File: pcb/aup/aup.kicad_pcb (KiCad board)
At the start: 8 copper layers, 81 x 50 mm, 83 parts, among them IC1 MT41K128M16JT-125_K, J1 QSH-060-01-L-D-A, J2 QSH-060-01-L-D-A, Q2 AO3400A, Q3 AO3401A, U1 XC7A50T-FGG484, U10 TPS2116DRLR, U11 FT2232HQ, U12 93LC56BT-I/OT, U13 MX25L3233FM2, U14 ISL80103IRAJZ-TK, U15 TPS2116DRLR, U2 USBLC6-2SC6, U5 TPS563257DRLR, U6 ISL80103IRAJZ-TK, U7 TPS563257DRLR, U8 TPS563257DRLR, U9 TPS563257DRLR, Y1 12MHz/20pf

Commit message: Add upper connector
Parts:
- added J3: QTH-060-01-L-D-A, !Misc:SAMTEC_QTH-060-01-X-D-A, B.Cu at (70.2, 75.0)
- added J4: QTH-060-01-L-D-A, !Misc:SAMTEC_QTH-060-01-X-D-A, B.Cu at (109.8, 75.0)
- added J5: QSH-030-01-L-D-A, !Misc:SAMTEC_QSH-030-01-X-D-A, F.Cu at (90.0, 55.4)
- added J6: QTH-030-01-L-D-A, !Misc:SAMTEC_QTH-030-01-X-D-A, B.Cu at (90.0, 55.4)
- moved FB1 138.7 mm to (264.4, 105.3)
- moved FB2 138.7 mm to (264.4, 109.3)
- moved R25 138.7 mm to (270.6, 94.2)
- moved R26 138.7 mm to (270.6, 90.7)
- moved U13 138.7 mm to (264.4, 75.4)
- moved Y1 138.7 mm to (276.4, 102.4)
- moved C1 138.7 mm to (165.0, 50.4)
- moved C11 138.7 mm to (196.8, 88.5)
- moved C12 138.7 mm to (196.8, 86.5)
- moved C13 138.7 mm to (193.9, 56.4)
- moved C14 138.7 mm to (200.0, 88.5)
- moved C15 138.7 mm to (193.8, 49.9)
- moved C16 138.7 mm to (203.4, 49.8)
- moved C17 138.7 mm to (203.6, 56.2)
- moved C19 138.7 mm to (198.2, 94.1)
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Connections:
- J1 pad 10: unconnected-(J1-Pad10) -> +3V3
- J1 pad 100: unconnected-(J1-Pad100) -> IOL_17B
- J1 pad 101: unconnected-(J1-Pad101) -> +3V3
- J1 pad 102: unconnected-(J1-Pad102) -> +3V3
- J1 pad 103: unconnected-(J1-Pad103) -> IOL_7A
- J1 pad 104: unconnected-(J1-Pad104) -> IOL_20B
- J1 pad 105: unconnected-(J1-Pad105) -> IOL_21A
- J1 pad 106: unconnected-(J1-Pad106) -> IOL_18B
- J1 pad 107: unconnected-(J1-Pad107) -> IOL_12A
- J1 pad 108: unconnected-(J1-Pad108) -> IOL_21B
- J1 pad 109: unconnected-(J1-Pad109) -> IOL_26B
- J1 pad 11: unconnected-(J1-Pad11) -> IOT_181
- J1 pad 110: unconnected-(J1-Pad110) -> IOL_24A
- J1 pad 111: unconnected-(J1-Pad111) -> +3V3
- J1 pad 112: unconnected-(J1-Pad112) -> +3V3
- J1 pad 113: unconnected-(J1-Pad113) -> IOL_25B
- J1 pad 114: unconnected-(J1-Pad114) -> IOL_25A
- J1 pad 115: unconnected-(J1-Pad115) -> IOL_16B
- J1 pad 116: unconnected-(J1-Pad116) -> IOL_26A
- J1 pad 117: unconnected-(J1-Pad117) -> IOL_22A
- J1 pad 118: unconnected-(J1-Pad118) -> IOL_22B
- J1 pad 119: unconnected-(J1-Pad119) -> IOL_19B
- J1 pad 12: unconnected-(J1-Pad12) -> IOT_182
- J1 pad 120: unconnected-(J1-Pad120) -> IOL_24B
- J1 pad 13: unconnected-(J1-Pad13) -> IOT_185
- J1 pad 14: unconnected-(J1-Pad14) -> IOT_187
- J1 pad 15: unconnected-(J1-Pad15) -> IOT_179
- J1 pad 16: unconnected-(J1-Pad16) -> IOT_169
- J1 pad 17: unconnected-(J1-Pad17) -> IOT_193
- J1 pad 18: unconnected-(J1-Pad18) -> IOT_184
- J1 pad 19: unconnected-(J1-Pad19) -> +3V3
- J1 pad 20: unconnected-(J1-Pad20) -> +3V3
- J1 pad 21: unconnected-(J1-Pad21) -> IOT_191
- J1 pad 22: unconnected-(J1-Pad22) -> IOT_168
- J1 pad 23: unconnected-(J1-Pad23) -> IOT_192
- J1 pad 24: unconnected-(J1-Pad24) -> IOT_186
- J1 pad 25: unconnected-(J1-Pad25) -> IOT_209
- J1 pad 26: unconnected-(J1-Pad26) -> IOT_183
- J1 pad 27: unconnected-(J1-Pad27) -> IOT_200
- J1 pad 28: unconnected-(J1-Pad28) -> IOT_194
- J1 pad 29: unconnected-(J1-Pad29) -> +3V3
- J1 pad 30: unconnected-(J1-Pad30) -> +3V3
- J1 pad 31: unconnected-(J1-Pad31) -> IOT_197
- J1 pad 32: unconnected-(J1-Pad32) -> IOT_177
- J1 pad 33: unconnected-(J1-Pad33) -> IOT_219
- J1 pad 34: unconnected-(J1-Pad34) -> IOT_199
- J1 pad 35: unconnected-(J1-Pad35) -> IOT_210
- J1 pad 36: unconnected-(J1-Pad36) -> IOT_203
- J1 pad 37: unconnected-(J1-Pad37) -> IOT_221
- J1 pad 38: unconnected-(J1-Pad38) -> IOT_205
- J1 pad 39: unconnected-(J1-Pad39) -> +3V3
- J1 pad 40: unconnected-(J1-Pad40) -> +3V3
- J1 pad 41: unconnected-(J1-Pad41) -> IOT_222
- J1 pad 42: unconnected-(J1-Pad42) -> IOT_207
- J1 pad 43: unconnected-(J1-Pad43) -> IOT_206
- J1 pad 44: unconnected-(J1-Pad44) -> IOT_211
- J1 pad 45: unconnected-(J1-Pad45) -> IOT_227
- J1 pad 46: unconnected-(J1-Pad46) -> IOT_208
- J1 pad 47: unconnected-(J1-Pad47) -> IOT_198
- J1 pad 48: unconnected-(J1-Pad48) -> IOT_216
- J1 pad 49: unconnected-(J1-Pad49) -> +3V3
- J1 pad 50: unconnected-(J1-Pad50) -> +3V3
- J1 pad 51: unconnected-(J1-Pad51) -> IOT_212
- J1 pad 52: unconnected-(J1-Pad52) -> IOT_213
- J1 pad 53: unconnected-(J1-Pad53) -> IOT_224
- J1 pad 54: unconnected-(J1-Pad54) -> IOT_214
- J1 pad 55: unconnected-(J1-Pad55) -> IOT_215
- J1 pad 56: unconnected-(J1-Pad56) -> IOT_223
- J1 pad 57: unconnected-(J1-Pad57) -> IOT_226
- J1 pad 58: unconnected-(J1-Pad58) -> IOT_218
- J1 pad 59: unconnected-(J1-Pad59) -> IOT_225
- J1 pad 60: unconnected-(J1-Pad60) -> IOT_220
- J1 pad 61: unconnected-(J1-Pad61) -> IOL_2A
- J1 pad 62: unconnected-(J1-Pad62) -> IOL_1B
- J1 pad 63: unconnected-(J1-Pad63) -> IOL_1A
- J1 pad 64: unconnected-(J1-Pad64) -> IOL_2B
- J1 pad 65: unconnected-(J1-Pad65) -> IOL_5A
- J1 pad 66: unconnected-(J1-Pad66) -> IOL_3B
- J1 pad 67: unconnected-(J1-Pad67) -> IOL_6B
- J1 pad 68: unconnected-(J1-Pad68) -> IOL_3A
- J1 pad 69: unconnected-(J1-Pad69) -> IOL_10A
- J1 pad 70: unconnected-(J1-Pad70) -> IOL_4B
- J1 pad 71: unconnected-(J1-Pad71) -> +3V3
- J1 pad 72: unconnected-(J1-Pad72) -> +3V3
- J1 pad 73: unconnected-(J1-Pad73) -> IOL_19A
- J1 pad 74: unconnected-(J1-Pad74) -> IOL_5B
- J1 pad 75: unconnected-(J1-Pad75) -> IOL_8B
- J1 pad 76: unconnected-(J1-Pad76) -> IOL_10B
- J1 pad 77: unconnected-(J1-Pad77) -> IOL_13A
- J1 pad 78: unconnected-(J1-Pad78) -> IOL_9B
- J1 pad 79: unconnected-(J1-Pad79) -> IOL_4A
- J1 pad 80: unconnected-(J1-Pad80) -> IOL_13B
- J1 pad 81: unconnected-(J1-Pad81) -> +3V3
- J1 pad 82: unconnected-(J1-Pad82) -> +3V3
- J1 pad 83: unconnected-(J1-Pad83) -> IOL_8A
- J1 pad 84: unconnected-(J1-Pad84) -> IOL_11B
- J1 pad 85: unconnected-(J1-Pad85) -> IOL_20A
- J1 pad 86: unconnected-(J1-Pad86) -> IOL_14B
- J1 pad 87: unconnected-(J1-Pad87) -> IOL_6A
- J1 pad 88: unconnected-(J1-Pad88) -> IOL_12B
- J1 pad 89: unconnected-(J1-Pad89) -> IOL_18A
- J1 pad 90: unconnected-(J1-Pad90) -> IOL_7B
- J1 pad 91: unconnected-(J1-Pad91) -> +3V3
- J1 pad 92: unconnected-(J1-Pad92) -> +3V3
- J1 pad 93: unconnected-(J1-Pad93) -> IOL_23A
- J1 pad 94: unconnected-(J1-Pad94) -> IOL_15B
- J1 pad 95: unconnected-(J1-Pad95) -> IOL_9A
- J1 pad 96: unconnected-(J1-Pad96) -> IOL_15A
- J1 pad 97: unconnected-(J1-Pad97) -> IOL_17A
- J1 pad 98: unconnected-(J1-Pad98) -> IOL_16A
- J1 pad 99: unconnected-(J1-Pad99) -> IOL_11A
- J2 pad 10: unconnected-(J2-Pad10) -> +3V3
- J2 pad 100: unconnected-(J2-Pad100) -> IOB_67
- J2 pad 101: unconnected-(J2-Pad101) -> +3V3
- J2 pad 102: unconnected-(J2-Pad102) -> +3V3
- J2 pad 103: unconnected-(J2-Pad103) -> IOB_75
- J2 pad 104: unconnected-(J2-Pad104) -> IOB_52
- J2 pad 105: unconnected-(J2-Pad105) -> IOB_53
- J2 pad 106: unconnected-(J2-Pad106) -> IOB_82
- J2 pad 107: unconnected-(J2-Pad107) -> IOB_73
- J2 pad 108: unconnected-(J2-Pad108) -> IOB_56
- J2 pad 109: unconnected-(J2-Pad109) -> IOB_71
- J2 pad 11: unconnected-(J2-Pad11) -> IOR_157
- J2 pad 110: unconnected-(J2-Pad110) -> IOB_77
- J2 pad 111: unconnected-(J2-Pad111) -> +3V3
- J2 pad 112: unconnected-(J2-Pad112) -> +3V3
- J2 pad 113: unconnected-(J2-Pad113) -> IOB_69
- J2 pad 114: unconnected-(J2-Pad114) -> IOB_64
- J2 pad 115: unconnected-(J2-Pad115) -> IOB_63
- J2 pad 116: unconnected-(J2-Pad116) -> IOB_54
- J2 pad 117: unconnected-(J2-Pad117) -> IOB_61
- J2 pad 118: unconnected-(J2-Pad118) -> IOB_58
- J2 pad 119: unconnected-(J2-Pad119) -> IOB_57
- J2 pad 12: unconnected-(J2-Pad12) -> IOR_160
- J2 pad 120: unconnected-(J2-Pad120) -> IOL_23B
- J2 pad 13: unconnected-(J2-Pad13) -> IOR_151
- J2 pad 14: unconnected-(J2-Pad14) -> IOR_150
- J2 pad 15: unconnected-(J2-Pad15) -> IOR_147
- J2 pad 16: unconnected-(J2-Pad16) -> IOR_155
- J2 pad 17: unconnected-(J2-Pad17) -> IOR_149
- J2 pad 18: unconnected-(J2-Pad18) -> IOR_146
- J2 pad 19: unconnected-(J2-Pad19) -> +3V3
- J2 pad 20: unconnected-(J2-Pad20) -> +3V3
- J2 pad 21: unconnected-(J2-Pad21) -> IOR_145
- J2 pad 22: unconnected-(J2-Pad22) -> IOR_144
- J2 pad 23: unconnected-(J2-Pad23) -> IOR_143
- J2 pad 24: unconnected-(J2-Pad24) -> IOR_152
- J2 pad 25: unconnected-(J2-Pad25) -> IOR_130
- J2 pad 26: unconnected-(J2-Pad26) -> IOR_140
- J2 pad 27: unconnected-(J2-Pad27) -> IOR_138
- J2 pad 28: unconnected-(J2-Pad28) -> IOR_142
- J2 pad 29: unconnected-(J2-Pad29) -> +3V3
- J2 pad 30: unconnected-(J2-Pad30) -> +3V3
- J2 pad 31: unconnected-(J2-Pad31) -> IOR_141
- J2 pad 32: unconnected-(J2-Pad32) -> IOR_139
- J2 pad 33: unconnected-(J2-Pad33) -> IOR_131
- J2 pad 34: unconnected-(J2-Pad34) -> IOR_136
- J2 pad 35: unconnected-(J2-Pad35) -> IOR_133
- J2 pad 36: unconnected-(J2-Pad36) -> IOR_122
- J2 pad 37: unconnected-(J2-Pad37) -> IOR_129
- J2 pad 38: unconnected-(J2-Pad38) -> IOR_126
- J2 pad 39: unconnected-(J2-Pad39) -> +3V3
- J2 pad 40: unconnected-(J2-Pad40) -> +3V3
- J2 pad 41: unconnected-(J2-Pad41) -> IOR_127
- J2 pad 42: unconnected-(J2-Pad42) -> IOR_116
- J2 pad 43: unconnected-(J2-Pad43) -> IOR_119
- J2 pad 44: unconnected-(J2-Pad44) -> IOR_137
- J2 pad 45: unconnected-(J2-Pad45) -> IOR_121
- J2 pad 46: unconnected-(J2-Pad46) -> IOR_114
- J2 pad 47: unconnected-(J2-Pad47) -> IOR_109
- J2 pad 48: unconnected-(J2-Pad48) -> IOR_134
- J2 pad 49: unconnected-(J2-Pad49) -> +3V3
- J2 pad 50: unconnected-(J2-Pad50) -> +3V3
- J2 pad 51: unconnected-(J2-Pad51) -> IOR_123
- J2 pad 52: unconnected-(J2-Pad52) -> IOR_120
- J2 pad 53: unconnected-(J2-Pad53) -> IOR_117
- J2 pad 54: unconnected-(J2-Pad54) -> IOR_115
- J2 pad 55: unconnected-(J2-Pad55) -> IOR_112
- J2 pad 56: unconnected-(J2-Pad56) -> IOR_128
- J2 pad 57: unconnected-(J2-Pad57) -> IOR_113
- J2 pad 58: unconnected-(J2-Pad58) -> IOR_111
- J2 pad 59: unconnected-(J2-Pad59) -> IOR_110
- J2 pad 60: unconnected-(J2-Pad60) -> IOR_118
- J2 pad 61: unconnected-(J2-Pad61) -> IOB_102
- J2 pad 62: unconnected-(J2-Pad62) -> IOB_101
- J2 pad 63: unconnected-(J2-Pad63) -> IOB_100
- J2 pad 64: unconnected-(J2-Pad64) -> IOB_98
- J2 pad 65: unconnected-(J2-Pad65) -> IOB_91
- J2 pad 66: unconnected-(J2-Pad66) -> IOB_93
- J2 pad 67: unconnected-(J2-Pad67) -> IOB_92
- J2 pad 68: unconnected-(J2-Pad68) -> IOB_105_SDO
- J2 pad 69: unconnected-(J2-Pad69) -> IOB_103_CBSEL1
- J2 pad 70: unconnected-(J2-Pad70) -> IOB_106_SDI
- J2 pad 71: unconnected-(J2-Pad71) -> +3V3
- J2 pad 72: unconnected-(J2-Pad72) -> +3V3
- J2 pad 73: unconnected-(J2-Pad73) -> IOB_60
- J2 pad 74: unconnected-(J2-Pad74) -> IOB_87
- J2 pad 75: unconnected-(J2-Pad75) -> IOB_94
- J2 pad 76: unconnected-(J2-Pad76) -> IOB_86
- J2 pad 77: unconnected-(J2-Pad77) -> IOB_107_SCK
- J2 pad 78: unconnected-(J2-Pad78) -> IOB_99
- J2 pad 79: unconnected-(J2-Pad79) -> IOB_89
- J2 pad 80: unconnected-(J2-Pad80) -> IOB_85
- J2 pad 81: unconnected-(J2-Pad81) -> +3V3
- J2 pad 82: unconnected-(J2-Pad82) -> +3V3
- J2 pad 83: unconnected-(J2-Pad83) -> IOB_84
- J2 pad 84: unconnected-(J2-Pad84) -> IOB_74
- J2 pad 85: unconnected-(J2-Pad85) -> IOB_88
- J2 pad 86: unconnected-(J2-Pad86) -> IOB_78
- J2 pad 87: unconnected-(J2-Pad87) -> IOB_81
- J2 pad 88: unconnected-(J2-Pad88) -> IOB_72
- J2 pad 89: unconnected-(J2-Pad89) -> IOB_59
- J2 pad 90: unconnected-(J2-Pad90) -> IOB_80
- J2 pad 91: unconnected-(J2-Pad91) -> +3V3
- J2 pad 92: unconnected-(J2-Pad92) -> +3V3
- J2 pad 93: unconnected-(J2-Pad93) -> IOB_79
- J2 pad 94: unconnected-(J2-Pad94) -> IOB_103_CBSEL0
- J2 pad 95: unconnected-(J2-Pad95) -> IOB_83
- J2 pad 96: unconnected-(J2-Pad96) -> IOB_66
- J2 pad 97: unconnected-(J2-Pad97) -> IOB_76
- J2 pad 98: unconnected-(J2-Pad98) -> IOB_68
- J2 pad 99: unconnected-(J2-Pad99) -> IOB_55
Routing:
- net +3V3: track 5.18 -> 116.6 mm, vias 7 -> 47
- net IOB_106_SDI: track 0.00 -> 22.5 mm, vias 0 -> 2
- net IOB_56: track 0.00 -> 20.8 mm, vias 0 -> 1
- net IOB_52: track 0.00 -> 20.7 mm, vias 0 -> 1
- net IOB_67: track 0.00 -> 20.6 mm, vias 0 -> 1
- net IOL_23B: track 0.00 -> 19.9 mm, vias 0 -> 1
- net IOB_54: track 0.00 -> 19.9 mm, vias 0 -> 1
- net IOB_66: track 0.00 -> 19.5 mm, vias 0 -> 1
- net IOB_72: track 0.00 -> 19.3 mm, vias 0 -> 1
- net IOB_74: track 0.00 -> 18.2 mm, vias 0 -> 1
- net IOR_150: track 0.00 -> 17.6 mm, vias 0 -> 1
- net IOB_85: track 0.00 -> 17.0 mm, vias 0 -> 1
- net IOR_148: track 0.00 -> 16.8 mm, vias 0 -> 1
- net IOR_154: track 0.00 -> 16.7 mm, vias 0 -> 1
- net IOR_136: track 0.00 -> 16.2 mm, vias 0 -> 1
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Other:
- board size 81 x 50 mm -> 80 x 50 mm

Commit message: Add hierarchical sheets for banks and add caps.
There are some stale sheets in this commit, but I don't want to delete
an active one accidentally. Save them all for now, and then go back and
clean them up.
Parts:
- added C10: 0.47uf, Capacitor_SMD:C_0402_1005Metric, B.Cu at (36.1, 68.0)
- added C18: 0.47uf, Capacitor_SMD:C_0402_1005Metric, B.Cu at (36.1, 66.1)
- added C2: 330uf, !Misc:T520V, B.Cu at (57.4, 96.3)
- added C20: 0.47uf, Capacitor_SMD:C_0402_1005Metric, F.Cu at (36.3, 0.48)
- added C23: 0.47uf, Capacitor_SMD:C_0402_1005Metric, B.Cu at (39.0, 73.9)
- added C3: 4.7uf, Capacitor_SMD:C_0805_2012Metric, F.Cu at (45.7, 1.00)
- added C34: 0.47uf, Capacitor_SMD:C_0402_1005Metric, B.Cu at (39.0, 72.0)
- added C35: 0.47uf, Capacitor_SMD:C_0402_1005Metric, B.Cu at (39.0, 70.0)
- added C36: 0.47uf, Capacitor_SMD:C_0402_1005Metric, B.Cu at (39.0, 68.0)
- added C4: 4.7uf, Capacitor_SMD:C_0805_2012Metric, F.Cu at (45.7, 4.01)
- added C41: 0.47uf, Capacitor_SMD:C_0402_1005Metric, B.Cu at (39.0, 66.1)
- added C42: 0.47uf, Capacitor_SMD:C_0402_1005Metric, B.Cu at (41.9, 75.9)
- added C45: 0.47uf, Capacitor_SMD:C_0402_1005Metric, F.Cu at (39.2, 2.46)
- added C46: 100uf, Capacitor_SMD:C_1206_3216Metric, F.Cu at (45.0, 13.0)
- added C47: 0.47uf, Capacitor_SMD:C_0402_1005Metric, F.Cu at (39.2, 4.42)
- added C48: 0.47uf, Capacitor_SMD:C_0402_1005Metric, F.Cu at (39.2, 6.39)
- added C49: 0.47uf, Capacitor_SMD:C_0402_1005Metric, F.Cu at (39.2, 8.37)
- added C5: 4.7uf, Capacitor_SMD:C_0805_2012Metric, F.Cu at (45.7, 7.03)
- added C51: 0.47uf, Capacitor_SMD:C_0402_1005Metric, F.Cu at (39.2, 10.3)
- added C52: 0.47uf, Capacitor_SMD:C_0402_1005Metric, F.Cu at (42.0, 0.48)
- added C53: 0.47uf, Capacitor_SMD:C_0402_1005Metric, F.Cu at (42.0, 2.46)
- added C54: 0.47uf, Capacitor_SMD:C_0402_1005Metric, F.Cu at (42.0, 4.42)
- added C55: 0.47uf, Capacitor_SMD:C_0402_1005Metric, F.Cu at (42.0, 6.39)
- added C56: 4.7uf, Capacitor_SMD:C_0805_2012Metric, F.Cu at (27.8, 1.00)
- added C57: 4.7uf, Capacitor_SMD:C_0805_2012Metric, F.Cu at (27.8, 4.01)
- added C58: 0.47uf, Capacitor_SMD:C_0402_1005Metric, F.Cu at (0.94, 26.5)
- added C59: 0.47uf, Capacitor_SMD:C_0402_1005Metric, F.Cu at (0.94, 28.5)
- added C6: 0.47uf, Capacitor_SMD:C_0402_1005Metric, B.Cu at (87.0, 71.5)
- added C60: 0.47uf, Capacitor_SMD:C_0402_1005Metric, F.Cu at (0.94, 30.5)
- added C61: 0.47uf, Capacitor_SMD:C_0402_1005Metric, F.Cu at (0.94, 32.4)
- added C62: 0.47uf, Capacitor_SMD:C_0402_1005Metric, F.Cu at (3.81, 26.5)
- added C63: 0.47uf, Capacitor_SMD:C_0402_1005Metric, F.Cu at (3.81, 28.5)
- added C64: 0.47uf, Capacitor_SMD:C_0402_1005Metric, F.Cu at (3.81, 30.5)
- added C65: 0.47uf, Capacitor_SMD:C_0402_1005Metric, F.Cu at (3.81, 32.4)
- added C66: 0.47uf, Capacitor_SMD:C_0402_1005Metric, F.Cu at (6.67, 26.5)
- added C67: 0.47uf, Capacitor_SMD:C_0402_1005Metric, F.Cu at (6.67, 28.5)
- added C68: 0.47uf, Capacitor_SMD:C_0402_1005Metric, F.Cu at (6.67, 30.5)
- added C69: 0.47uf, Capacitor_SMD:C_0402_1005Metric, F.Cu at (6.67, 32.4)
- added C7: 0.47uf, Capacitor_SMD:C_0402_1005Metric, B.Cu at (36.1, 73.9)
- added C70: 4.7uf, Capacitor_SMD:C_0805_2012Metric, F.Cu at (27.8, 7.03)
- added C71: 4.7uf, Capacitor_SMD:C_0805_2012Metric, F.Cu at (27.8, 10.0)
- added C72: 47uf, Capacitor_SMD:C_1206_3216Metric, F.Cu at (10.9, 27.2)
- added C73: 0.47uf, Capacitor_SMD:C_0402_1005Metric, F.Cu at (33.4, 33.7)
- added C74: 0.47uf, Capacitor_SMD:C_0402_1005Metric, F.Cu at (37.9, 19.7)
- added C75: 0.47uf, Capacitor_SMD:C_0402_1005Metric, F.Cu at (33.4, 35.7)
- added C76: 0.47uf, Capacitor_SMD:C_0402_1005Metric, F.Cu at (37.9, 21.7)
- added C77: 0.47uf, Capacitor_SMD:C_0402_1005Metric, F.Cu at (33.4, 37.7)
- added C78: 0.47uf, Capacitor_SMD:C_0402_1005Metric, F.Cu at (37.9, 23.6)
- added C79: 0.47uf, Capacitor_SMD:C_0402_1005Metric, F.Cu at (33.4, 39.7)
- added C8: 0.47uf, Capacitor_SMD:C_0402_1005Metric, B.Cu at (36.1, 72.0)
- added C80: 0.47uf, Capacitor_SMD:C_0402_1005Metric, F.Cu at (37.9, 25.6)
- added C81: 0.47uf, Capacitor_SMD:C_0402_1005Metric, F.Cu at (33.4, 41.6)
- added C82: 0.47uf, Capacitor_SMD:C_0402_1005Metric, F.Cu at (40.8, 19.7)
- added C83: 0.47uf, Capacitor_SMD:C_0402_1005Metric, F.Cu at (33.4, 43.6)
- added C84: 0.47uf, Capacitor_SMD:C_0402_1005Metric, F.Cu at (40.8, 21.7)
- added C85: 4.7uf, Capacitor_SMD:C_0805_2012Metric, F.Cu at (37.1, 34.3)
- added C86: 4.7uf, Capacitor_SMD:C_0805_2012Metric, F.Cu at (34.2, 20.2)
- added C87: 47uf, Capacitor_SMD:C_1206_3216Metric, F.Cu at (37.7, 40.5)
- added C88: 4.7uf, Capacitor_SMD:C_0805_2012Metric, F.Cu at (37.1, 37.3)
- added C89: 47uf, Capacitor_SMD:C_1206_3216Metric, F.Cu at (39.3, 28.3)
- added C9: 0.47uf, Capacitor_SMD:C_0402_1005Metric, B.Cu at (36.1, 70.0)
- added C90: 4.7uf, Capacitor_SMD:C_0805_2012Metric, F.Cu at (34.2, 23.2)
- added C91: 0.47uf, Capacitor_SMD:C_0402_1005Metric, F.Cu at (40.8, 23.6)
- added C92: 0.47uf, Capacitor_SMD:C_0402_1005Metric, F.Cu at (40.8, 25.6)
- added C93: 0.47uf, Capacitor_SMD:C_0402_1005Metric, F.Cu at (43.6, 19.7)
- added C94: 0.47uf, Capacitor_SMD:C_0402_1005Metric, F.Cu at (43.6, 21.7)
- added C95: 0.47uf, Capacitor_SMD:C_0402_1005Metric, F.Cu at (43.6, 23.6)
- added C96: 0.47uf, Capacitor_SMD:C_0402_1005Metric, F.Cu at (43.6, 25.6)
- added C97: 4.7uf, Capacitor_SMD:C_0805_2012Metric, F.Cu at (34.2, 26.2)
- added C98: 4.7uf, Capacitor_SMD:C_0805_2012Metric, F.Cu at (34.2, 29.3)
- FB1, FB2: value FB_600_805 -> 600/200ma; footprint Inductor_SMD:L_0805_2012Metric -> Inductor_SMD:L_0603_1608Metric
- U1: value XC7A50T-FGG484 -> XC7A50T-2FGG484C
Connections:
- U1 pad AA17: +3V3 -> GND
- U1 pad AB14: +3V3 -> GND
- U1 pad E12: unconnected-(U1G-VCCBATT_0-PadE12) -> +1V0
- U1 pad V16: +3V3 -> GND
- U1 pad W13: +3V3 -> GND
- U1 pad Y10: +3V3 -> GND

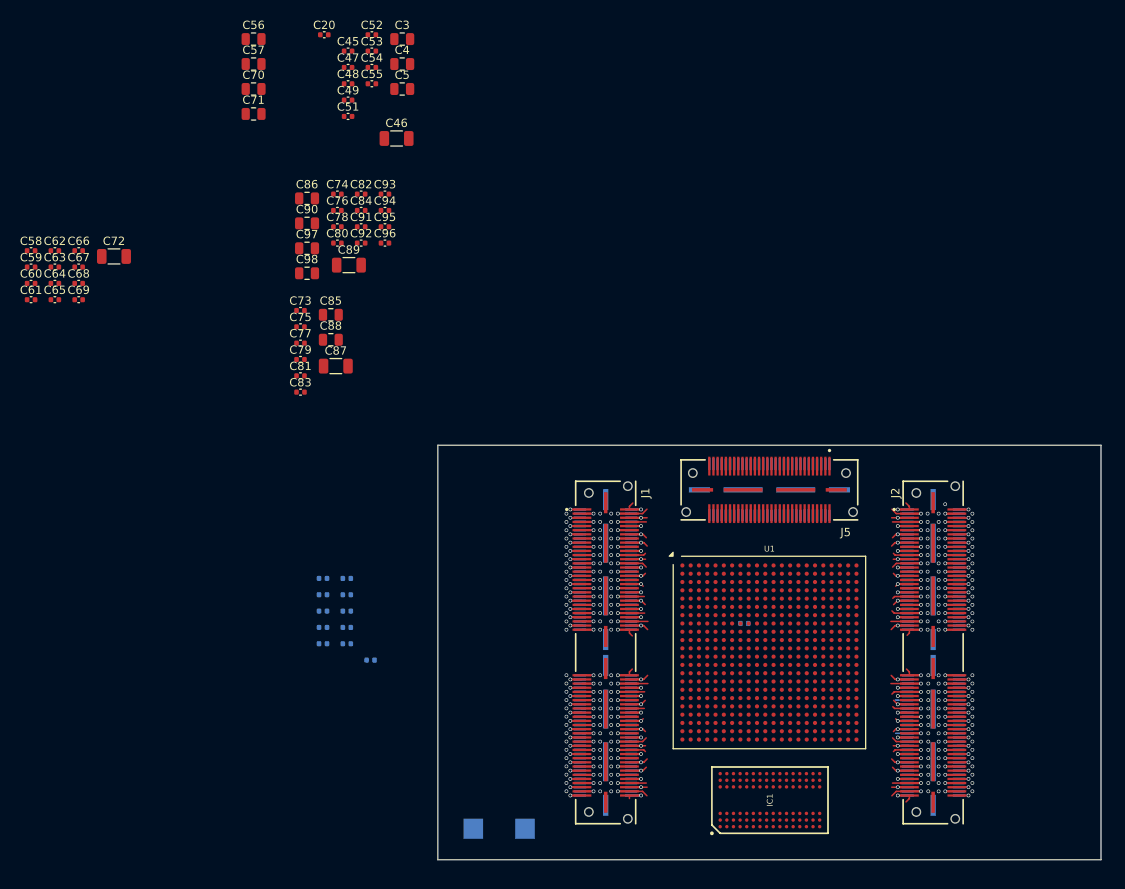
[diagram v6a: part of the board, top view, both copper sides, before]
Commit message: Added more passives
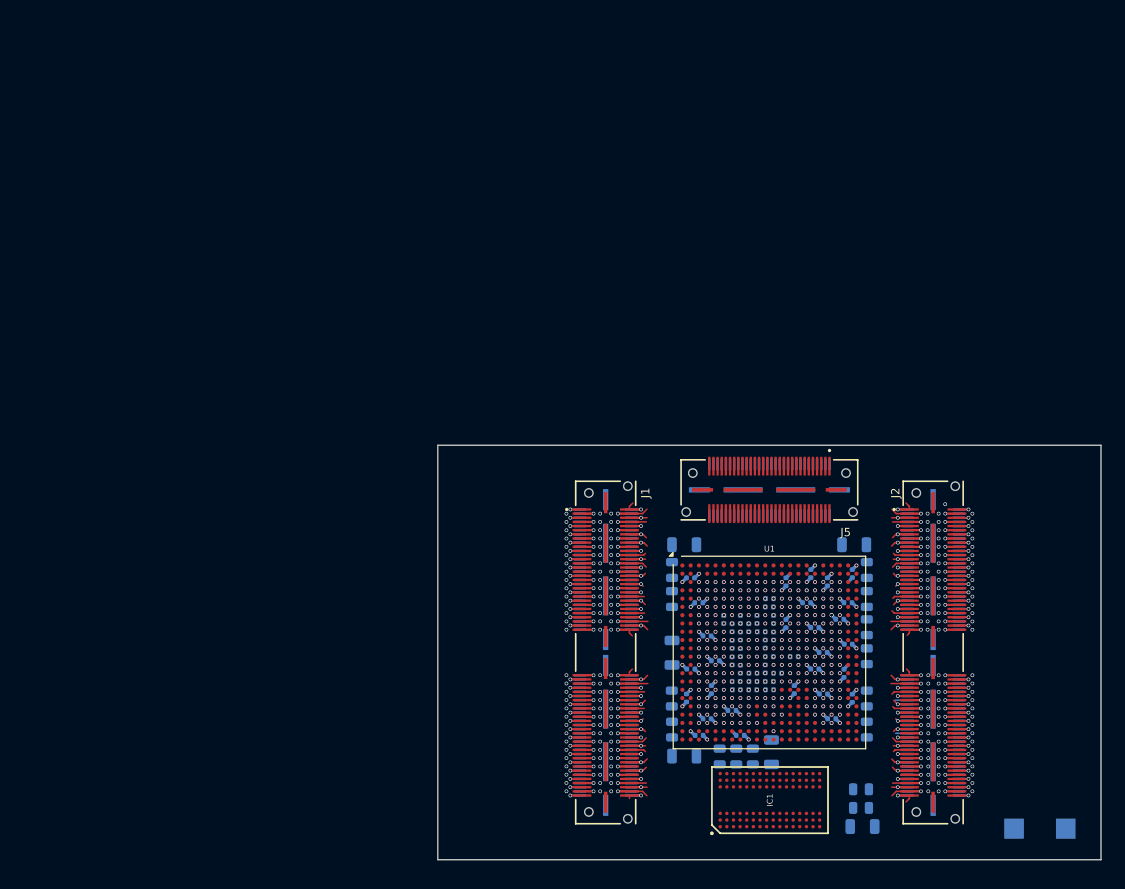
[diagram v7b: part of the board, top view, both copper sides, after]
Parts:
- added C100: 4.7uf, Capacitor_SMD:C_0805_2012Metric, B.Cu at (101.0, 93.8)
- added C101: 47uf, Capacitor_SMD:C_1206_3216Metric, B.Cu at (101.2, 96.0)
- added C102: 0.47uf, Capacitor_SMD:C_0402_1005Metric, B.Cu at (90.0, 79.5)
- added C103: 0.47uf, Capacitor_SMD:C_0402_1005Metric, B.Cu at (90.0, 69.5)
- added C104: 47uf, Capacitor_SMD:C_1206_3216Metric, B.Cu at (78.2, 75.0)
- added C50: 0.47uf, Capacitor_SMD:C_0402_1005Metric, B.Cu at (90.0, 68.5)
- added C99: 4.7uf, Capacitor_SMD:C_0805_2012Metric, B.Cu at (101.0, 91.5)
- C20, C3, C4, C45, C46, C47, C48, C49, C5, C51, C52, C53, C54, C55, C56, C57, C58, C59, C60, C61, C62, C63, C64, C65, C66, C67, C68, C69, C70, C71, C72, C73, C74, C75, C76, C77, C78, C79, C80, C81, C82, C83, C84, C85, C86, C87, C88, C89, C90, C91, C92, C93, C94, C95, C96, C97, C98: moved to B.Cu
- moved C58 107.2 mm to (98.5, 71.0)
- moved C63 107.1 mm to (99.0, 77.5), turned to -90 degrees
- moved C61 107.0 mm to (99.5, 74.0)
- moved C62 104.6 mm to (96.5, 75.0)
- moved C59 104.1 mm to (95.5, 72.0)
- moved C66 101.1 mm to (100.0, 65.5), turned to 90 degrees
- moved C57 100.4 mm to (101.8, 71.9), turned to 90 degrees
- moved C60 99.9 mm to (92.0, 71.5), turned to 90 degrees
- moved C69 99.7 mm to (99.5, 69.0), turned to 180 degrees
- moved C71 98.7 mm to (101.8, 75.4), turned to 90 degrees
- moved C67 98.0 mm to (97.0, 66.5), turned to 90 degrees
- moved C56 97.8 mm to (101.8, 65.1), turned to 90 degrees
- moved C64 97.7 mm to (95.0, 65.5), turned to -90 degrees
- moved C70 96.2 mm to (101.8, 68.6), turned to 90 degrees
- moved C68 95.9 mm to (94.5, 69.0)
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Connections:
- U1 pad F12: unconnected-(U1F-VCCO_0-PadF12) -> +3V3
- U1 pad T12: unconnected-(U1F-VCCO_0-PadT12) -> +3V3
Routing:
- net GND: track 13.7 -> 34.3 mm, vias 235 -> 314
- net +Vsel: track 0.00 -> 8.69 mm, vias 0 -> 10
- net +3V3: track 116.6 -> 123.8 mm, vias 47 -> 61
- net +1V35: track 0.00 -> 4.07 mm, vias 9 -> 14
- net unconnected-(U1F-VP_0-PadL10): vias 0 -> 1
- net unconnected-(U1F-VN_0-PadM9): vias 0 -> 1
- net unconnected-(U1F-TDO_0-PadU13): vias 0 -> 1
- net unconnected-(U1F-TDI_0-PadR13): vias 0 -> 1
- net unconnected-(U1F-TCK_0-PadV12): vias 0 -> 1
- net unconnected-(U1F-PROGRAM_B_0-PadN12): vias 0 -> 1
- net unconnected-(U1F-M2_0-PadU9): vias 0 -> 1
- net unconnected-(U1F-M1_0-PadU10): vias 0 -> 1
- net unconnected-(U1F-M0_0-PadU11): vias 0 -> 1
- net unconnected-(U1F-INIT_B_0-PadU12): vias 0 -> 1
- net unconnected-(U1F-DXP_0-PadN10): vias 0 -> 1
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- added copper zone on In3.Cu, net +Vsel
